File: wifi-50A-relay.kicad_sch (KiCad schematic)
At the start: 40 parts, among them J1 PROG, J2 100k_HOT, J3 100k_COLD, K1 J115F21C12VDCS.9, K2 J115F21C12VDCS.9, Q1 AO3400A, SW1 SKRKAEE020, U1 ESP-WROOM-02, U2 TPS54331DR, U3 ADS1115IDGS

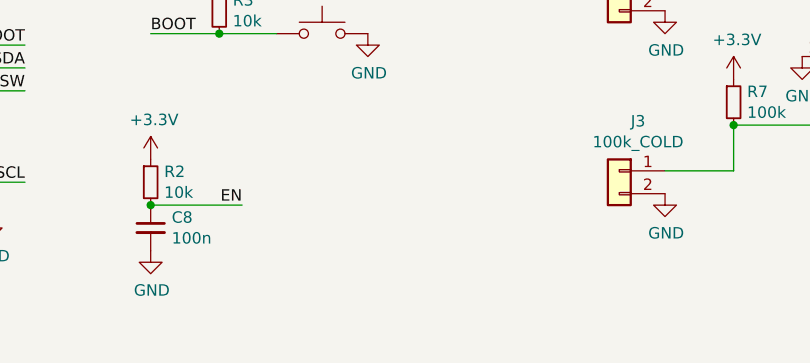
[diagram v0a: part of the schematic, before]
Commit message: Add i2c pull-ups
Forgotten in previous revisions
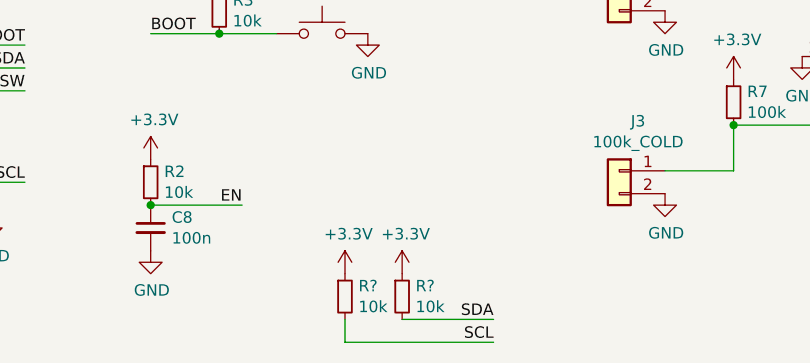
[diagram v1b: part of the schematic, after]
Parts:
- added R? (x2): 10k, Resistor_SMD:R_0402_1005Metric, symbol Device:R_Small
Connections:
- net +3V3: now also R?.1, R?.1
- net SCL: now also R?.2
- net SDA: now also R?.2
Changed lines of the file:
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@@
+    (stroke (width 0) (type default) (color 0 0 0 0))
+  )
+  (wire (pts (xy 118.11 168.91) (xy 118.11 171.45))
     (stroke (width 0) (type default) (color 0 0 0 0))
   )
@@
     (stroke (width 0) (type default) (color 0 0 0 0))
   )
+  (wire (pts (xy 124.46 168.91) (xy 134.62 168.91))
+    (stroke (width 0) (type default) (color 0 0 0 0))
+  )
   (wire (pts (xy 198.12 113.03) (xy 207.01 113.03))
     (stroke (width 0) (type default) (color 0 0 0 0))
@@
   )
   (wire (pts (xy 182.88 57.15) (xy 191.77 57.15))
+    (stroke (width 0) (type default) (color 0 0 0 0))
+  )
+  (wire (pts (xy 118.11 171.45) (xy 134.62 171.45))
     (stroke (width 0) (type default) (color 0 0 0 0))
   )
@@
     (effects (font (size 1.27 1.27)) (justify left bottom))
   )
+  (label "SDA" (at 134.62 168.91 180)
+    (effects (font (size 1.27 1.27)) (justify right bottom))
+  )
   (label "1.65V" (at 212.09 134.62 0)
     (effects (font (size 1.27 1.27)) (justify left bottom))
+  )
+  (label "SCL" (at 134.62 171.45 180)
+    (effects (font (size 1.27 1.27)) (justify right bottom))
   )
   (label "AC_PH_1" (at 38.1 34.29 0)
@@
     (pin "1")
   )
+  (symbol (lib_id "Device:R_Small") (at 118.11 166.37 0) (unit 1)
+    (in_bom yes) (on_board yes)
+    (property "Reference" "R?" (id 0) (at 119.6086 165.2016 0)
+      (effects (font (size 1.27 1.27)) (justify left))
+    )
+    (property "Value" "10k" (id 1) (at 119.6086 167.513 0)
+      (effects (font (size 1.27 1.27)) (justify left))
+    )
+    (property "Footprint" "Resistor_SMD:R_0402_1005Metric" (id 2) (at 118.11 166.37 0)
+      (effects (font (size 1.27 1.27)) hide)
+    )
+    (property "Datasheet" "~" (id 3) (at 118.11 166.37 0)
+      (effects (font (size 1.27 1.27)) hide)
+    )
+    (property "LCSC" "C25744" (id 4) (at 118.11 166.37 0)
+      (effects (font (size 1.27 1.27)) hide)
+    )
+    (pin "1")
+    (pin "2")
+  )
+  (symbol (lib_id "Device:R_Small") (at 124.46 166.37 0) (unit 1)
+    (in_bom yes) (on_board yes)
+    (property "Reference" "R?" (id 0) (at 125.9586 165.2016 0)
+      (effects (font (size 1.27 1.27)) (justify left))
+    )
+    (property "Value" "10k" (id 1) (at 125.9586 167.513 0)
+      (effects (font (size 1.27 1.27)) (justify left))
+    )
+    (property "Footprint" "Resistor_SMD:R_0402_1005Metric" (id 2) (at 124.46 166.37 0)
+      (effects (font (size 1.27 1.27)) hide)
+    )
+    (property "Datasheet" "~" (id 3) (at 124.46 166.37 0)
+      (effects (font (size 1.27 1.27)) hide)
+    )
+    (property "LCSC" "C25744" (id 4) (at 124.46 166.37 0)
+      (effects (font (size 1.27 1.27)) hide)
+    )
+    (pin "1")
+    (pin "2")
+  )
+  (symbol (lib_id "power:+3.3V") (at 124.46 163.83 0) (unit 1)
+    (in_bom yes) (on_board yes)
+    (property "Reference" "#PWR?" (id 0) (at 124.46 167.64 0)
+      (effects (font (size 1.27 1.27)) hide)
+    )
+    (property "Value" "+3.3V" (id 1) (at 124.841 159.4358 0))
+    (property "Footprint" "" (id 2) (at 124.46 163.83 0)
+      (effects (font (size 1.27 1.27)) hide)
+    )
+    (property "Datasheet" "" (id 3) (at 124.46 163.83 0)
+      (effects (font (size 1.27 1.27)) hide)
+    )
+    (pin "1")
+  )
+  (symbol (lib_id "power:+3.3V") (at 118.11 163.83 0) (unit 1)
+    (in_bom yes) (on_board yes)
+    (property "Reference" "#PWR?" (id 0) (at 118.11 167.64 0)
+      (effects (font (size 1.27 1.27)) hide)
+    )
+    (property "Value" "+3.3V" (id 1) (at 118.491 159.4358 0))
+    (property "Footprint" "" (id 2) (at 118.11 163.83 0)
+      (effects (font (size 1.27 1.27)) hide)
+    )
+    (property "Datasheet" "" (id 3) (at 118.11 163.83 0)
+      (effects (font (size 1.27 1.27)) hide)
+    )
+    (pin "1")
+  )
   (symbol (lib_id "power:GND") (at 78.74 157.48 0) (unit 1)
     (in_bom yes) (on_board yes)
@@
       (reference "#PWR0138") (unit 1) (value "GND") (footprint "")
     )
+    (path "/66d293a2-3353-44ee-87f9-05f057b5eb84"
+      (reference "#PWR?") (unit 1) (value "+3.3V") (footprint "")
+    )
+    (path "/bea48247-76c1-43f2-8bbc-503fcfa459d6"
+      (reference "#PWR?") (unit 1) (value "+3.3V") (footprint "")
+    )
     (path "/00000000-0000-0000-0000-00006120e737"
       (reference "#SYM1") (unit 1) (value "SYM_Flash_Large") (footprint "")
@@
       (reference "R12") (unit 1) (value "10k") (footprint "Resistor_SMD:R_0402_1005Metric")
     )
+    (path "/41c2e72d-689c-4d75-9887-ab0b28f392e9"
+      (reference "R?") (unit 1) (value "10k") (footprint "Resistor_SMD:R_0402_1005Metric")
+    )
+    (path "/474ececd-6a56-420e-b707-ed1bfb009c23"
+      (reference "R?") (unit 1) (value "10k") (footprint "Resistor_SMD:R_0402_1005Metric")
+    )
     (path "/00000000-0000-0000-0000-0000611a938f"

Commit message: Fix erc issues
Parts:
- L1: symbol Device:L_Core_Ferrite -> Device:L_Ferrite
- gave numbers to parts that had none: 2
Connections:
- net +3V3 renamed +3.3V

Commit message: Replace hand-soldered connectors with JST-XH
These seem to be the most common connector for the 3950 100k NTC
connectors found in 3d printers.
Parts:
- J2, J3: footprint Connector_Wire:SolderWire-0.25sqmm_1x02_P4.2mm_D0.65mm_OD1.7mm -> Connector_JST:JST_XH_B2B-XH-AM_1x02_P2.50mm_Vertical; LCSC (none) -> C2979476
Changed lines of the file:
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@@
     (property "Reference" "J2" (id 0) (at 150.6728 126.5682 0))
     (property "Value" "100k_HOT" (id 1) (at 150.6728 128.8796 0))
-    (property "Footprint" "Connector_Wire:SolderWire-0.25sqmm_1x02_P4.2mm_D0.65mm_OD1.7mm" (id 2) (at 148.59 132.08 0)
+    (property "Footprint" "Connector_JST:JST_XH_B2B-XH-AM_1x02_P2.50mm_Vertical" (id 2) (at 148.59 132.08 0)
       (effects (font (size 1.27 1.27)) hide)
     )
     (property "Datasheet" "~" (id 3) (at 148.59 132.08 0)
+      (effects (font (size 1.27 1.27)) hide)
+    )
+    (property "LCSC" "C2979476" (id 4) (at 148.59 132.08 0)
       (effects (font (size 1.27 1.27)) hide)
     )
@@
     (property "Reference" "J3" (id 0) (at 150.6728 146.8882 0))
     (property "Value" "100k_COLD" (id 1) (at 150.6728 149.1996 0))
-    (property "Footprint" "Connector_Wire:SolderWire-0.25sqmm_1x02_P4.2mm_D0.65mm_OD1.7mm" (id 2) (at 148.59 152.4 0)
+    (property "Footprint" "Connector_JST:JST_XH_B2B-XH-AM_1x02_P2.50mm_Vertical" (id 2) (at 148.59 152.4 0)
       (effects (font (size 1.27 1.27)) hide)
     )
     (property "Datasheet" "~" (id 3) (at 148.59 152.4 0)
+      (effects (font (size 1.27 1.27)) hide)
+    )
+    (property "LCSC" "C2979476" (id 4) (at 148.59 152.4 0)
       (effects (font (size 1.27 1.27)) hide)
     )
@@
     )
     (path "/00000000-0000-0000-0000-00006127360e"
-      (reference "J2") (unit 1) (value "100k_HOT") (footprint "Connector_Wire:SolderWire-0.25sqmm_1x02_P4.2mm_D0.65mm_OD1.7mm")
+      (reference "J2") (unit 1) (value "100k_HOT") (footprint "Connector_JST:JST_XH_B2B-XH-AM_1x02_P2.50mm_Vertical")
     )
     (path "/00000000-0000-0000-0000-000061286fe7"
-      (reference "J3") (unit 1) (value "100k_COLD") (footprint "Connector_Wire:SolderWire-0.25sqmm_1x02_P4.2mm_D0.65mm_OD1.7mm")
+      (reference "J3") (unit 1) (value "100k_COLD") (footprint "Connector_JST:JST_XH_B2B-XH-AM_1x02_P2.50mm_Vertical")
     )
     (path "/00000000-0000-0000-0000-000061161134"
